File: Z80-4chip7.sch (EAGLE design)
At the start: 99 parts, among them IC1 Z84C00xx (-Z80-), IC2 CXK581000 (128k * 8), IC4 7400N, M1 WIRE-VIA8, U1 ATMEGA32A-PU

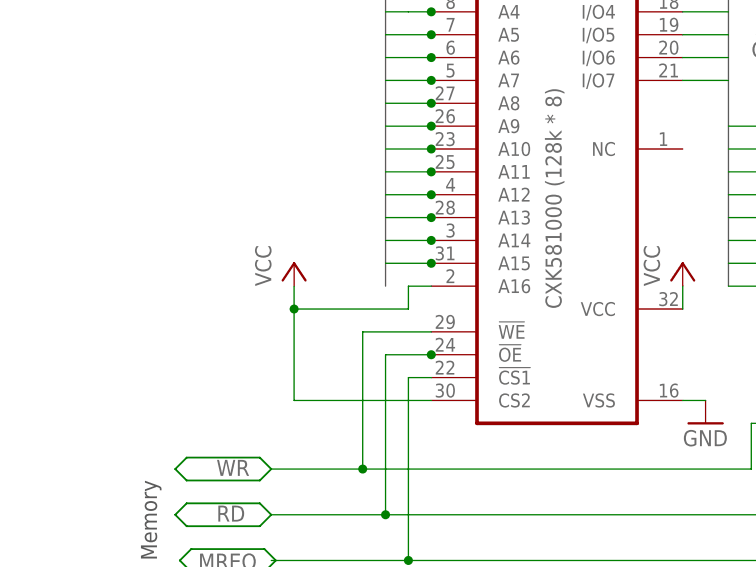
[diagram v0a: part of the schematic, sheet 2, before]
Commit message: Mod silkscreen: RTS->DTR, add "Version 2."  Generate Gerbers-V2.
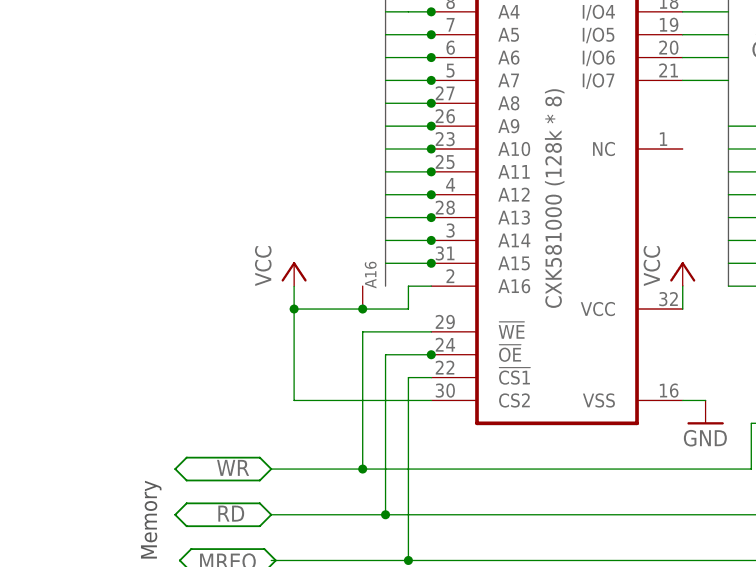
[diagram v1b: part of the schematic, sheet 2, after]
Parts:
- added A16: WIRE-VIA8, mylib4:WIRE-VIA8
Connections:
- net VCC: now also A16.P$1
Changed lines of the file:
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@@
 <grid distance="0.1" unitdist="inch" unit="mm" style="lines" multiple="1" display="no" altdistance="0.01" altunitdist="inch" altunit="inch"/>
 <layers>
-<layer number="1" name="Top" color="4" fill="1" visible="yes" active="no"/>
-<layer number="2" name="Route2" color="1" fill="3" visible="yes" active="no"/>
-<layer number="3" name="Route3" color="4" fill="3" visible="yes" active="no"/>
-<layer number="14" name="Route14" color="1" fill="6" visible="yes" active="no"/>
-<layer number="15" name="Route15" color="4" fill="6" visible="yes" active="no"/>
-<layer number="16" name="Bottom" color="1" fill="1" visible="yes" active="no"/>
-<layer number="17" name="Pads" color="2" fill="1" visible="yes" active="no"/>
-<layer number="18" name="Vias" color="2" fill="1" visible="yes" active="no"/>
-<layer number="19" name="Unrouted" color="6" fill="1" visible="yes" active="no"/>
-<layer number="20" name="Dimension" color="15" fill="1" visible="yes" active="no"/>
-<layer number="21" name="tPlace" color="7" fill="1" visible="yes" active="no"/>
-<layer number="22" name="bPlace" color="7" fill="1" visible="yes" active="no"/>
-<layer number="23" name="tOrigins" color="15" fill="1" visible="yes" active="no"/>
-<layer number="24" name="bOrigins" color="15" fill="1" visible="yes" active="no"/>
-<layer number="25" name="tNames" color="7" fill="1" visible="yes" active="no"/>
-<layer number="26" name="bNames" color="7" fill="1" visible="yes" active="no"/>
-<layer number="27" name="tValues" color="7" fill="1" visible="yes" active="no"/>
-<layer number="28" name="bValues" color="7" fill="1" visible="yes" active="no"/>
+<layer number="1" name="Top" color="4" fill="1" visible="no" active="no"/>
+<layer number="2" name="Route2" color="1" fill="3" visible="no" active="no"/>
+<layer number="3" name="Route3" color="4" fill="3" visible="no" active="no"/>
+<layer number="14" name="Route14" color="1" fill="6" visible="no" active="no"/>
+<layer number="15" name="Route15" color="4" fill="6" visible="no" active="no"/>
+<layer number="16" name="Bottom" color="1" fill="1" visible="no" active="no"/>
+<layer number="17" name="Pads" color="2" fill="1" visible="no" active="no"/>
+<layer number="18" name="Vias" color="2" fill="1" visible="no" active="no"/>
+<layer number="19" name="Unrouted" color="6" fill="1" visible="no" active="no"/>
+<layer number="20" name="Dimension" color="15" fill="1" visible="no" active="no"/>
+<layer number="21" name="tPlace" color="7" fill="1" visible="no" active="no"/>
+<layer number="22" name="bPlace" color="7" fill="1" visible="no" active="no"/>
+<layer number="23" name="tOrigins" color="15" fill="1" visible="no" active="no"/>
+<layer number="24" name="bOrigins" color="15" fill="1" visible="no" active="no"/>
+<layer number="25" name="tNames" color="7" fill="1" visible="no" active="no"/>
+<layer number="26" name="bNames" color="7" fill="1" visible="no" active="no"/>
+<layer number="27" name="tValues" color="7" fill="1" visible="no" active="no"/>
+<layer number="28" name="bValues" color="7" fill="1" visible="no" active="no"/>
 <layer number="29" name="tStop" color="7" fill="3" visible="no" active="no"/>
 <layer number="30" name="bStop" color="7" fill="6" visible="no" active="no"/>
@@
 <layer number="35" name="tGlue" color="7" fill="4" visible="no" active="no"/>
 <layer number="36" name="bGlue" color="7" fill="5" visible="no" active="no"/>
-<layer number="37" name="tTest" color="7" fill="1" visible="yes" active="no"/>
-<layer number="38" name="bTest" color="7" fill="1" visible="yes" active="no"/>
+<layer number="37" name="tTest" color="7" fill="1" visible="no" active="no"/>
+<layer number="38" name="bTest" color="7" fill="1" visible="no" active="no"/>
 <layer number="39" name="tKeepout" color="4" fill="11" visible="no" active="no"/>
 <layer number="40" name="bKeepout" color="1" fill="11" visible="no" active="no"/>
@@
 <layer number="44" name="Drills" color="7" fill="1" visible="no" active="no"/>
 <layer number="45" name="Holes" color="7" fill="1" visible="no" active="no"/>
-<layer number="46" name="Milling" color="3" fill="1" visible="yes" active="no"/>
-<layer number="47" name="Measures" color="7" fill="1" visible="yes" active="no"/>
-<layer number="48" name="Document" color="7" fill="1" visible="yes" active="no"/>
-<layer number="49" name="Reference" color="7" fill="1" visible="yes" active="no"/>
-<layer number="50" name="dxf" color="7" fill="1" visible="yes" active="no"/>
-<layer number="51" name="tDocu" color="7" fill="1" visible="yes" active="no"/>
-<layer number="52" name="bDocu" color="7" fill="1" visible="yes" active="no"/>
-<layer number="53" name="tGND_GNDA" color="7" fill="9" visible="yes" active="no"/>
-<layer number="54" name="bGND_GNDA" color="1" fill="9" visible="yes" active="no"/>
-<layer number="56" name="wert" color="7" fill="1" visible="yes" active="no"/>
-<layer number="57" name="tCAD" color="7" fill="1" visible="yes" active="no"/>
+<layer number="46" name="Milling" color="3" fill="1" visible="no" active="no"/>
+<layer number="47" name="Measures" color="7" fill="1" visible="no" active="no"/>
+<layer number="48" name="Document" color="7" fill="1" visible="no" active="no"/>
+<layer number="49" name="Reference" color="7" fill="1" visible="no" active="no"/>
+<layer number="50" name="dxf" color="7" fill="1" visible="no" active="no"/>
+<layer number="51" name="tDocu" color="7" fill="1" visible="no" active="no"/>
+<layer number="52" name="bDocu" color="7" fill="1" visible="no" active="no"/>
+<layer number="53" name="tGND_GNDA" color="7" fill="9" visible="no" active="no"/>
+<layer number="54" name="bGND_GNDA" color="1" fill="9" visible="no" active="no"/>
+<layer number="56" name="wert" color="7" fill="1" visible="no" active="no"/>
+<layer number="57" name="tCAD" color="7" fill="1" visible="no" active="no"/>
 <layer number="90" name="Modules" color="5" fill="1" visible="yes" active="yes"/>
 <layer number="91" name="Nets" color="2" fill="1" visible="yes" active="yes"/>
@@
 <part name="W3" library="mylib4" deviceset="WIRE" device="-R10" value="WIRE-R10"/>
 <part name="W4" library="mylib4" deviceset="WIRE" device="-R10" value="WIRE-R10"/>
+<part name="A16" library="mylib4" deviceset="WIRE" device="-VIA8"/>
 </parts>
 <sheets>
@@
 </instance>
 <instance part="U$26" gate="G$1" x="132.08" y="27.94" smashed="yes"/>
+<instance part="A16" gate="G$1" x="0" y="27.94" smashed="yes" rot="R90">
+<attribute name="NAME" x="0.254" y="30.226" size="1.27" layer="95" rot="MR90"/>
+</instance>
 </instances>
 <busses>
@@
 <wire x1="7.62" y1="30.48" x2="5.08" y2="30.48" width="0.1524" layer="91"/>
 <wire x1="5.08" y1="30.48" x2="5.08" y2="27.94" width="0.1524" layer="91"/>
-<wire x1="5.08" y1="27.94" x2="-7.62" y2="27.94" width="0.1524" layer="91"/>
+<wire x1="5.08" y1="27.94" x2="0" y2="27.94" width="0.1524" layer="91"/>
 <pinref part="P+13" gate="VCC" pin="VCC"/>
+<wire x1="0" y1="27.94" x2="-7.62" y2="27.94" width="0.1524" layer="91"/>
 <wire x1="-7.62" y1="30.48" x2="-7.62" y2="27.94" width="0.1524" layer="91"/>
 <junction x="-7.62" y="27.94"/>
-</segment>
-<segment>
+<pinref part="A16" gate="G$1" pin="P$1"/>
+<junction x="0" y="27.94"/>
+</segment>
+<segment>
